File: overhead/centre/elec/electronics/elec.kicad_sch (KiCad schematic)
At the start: 135 parts, among them IC1 MAX7219CWG, J1 Conn_02x01, J2 Conn_02x20_Counter_Clockwise, P1 Conn_01x02, P2 DataIn

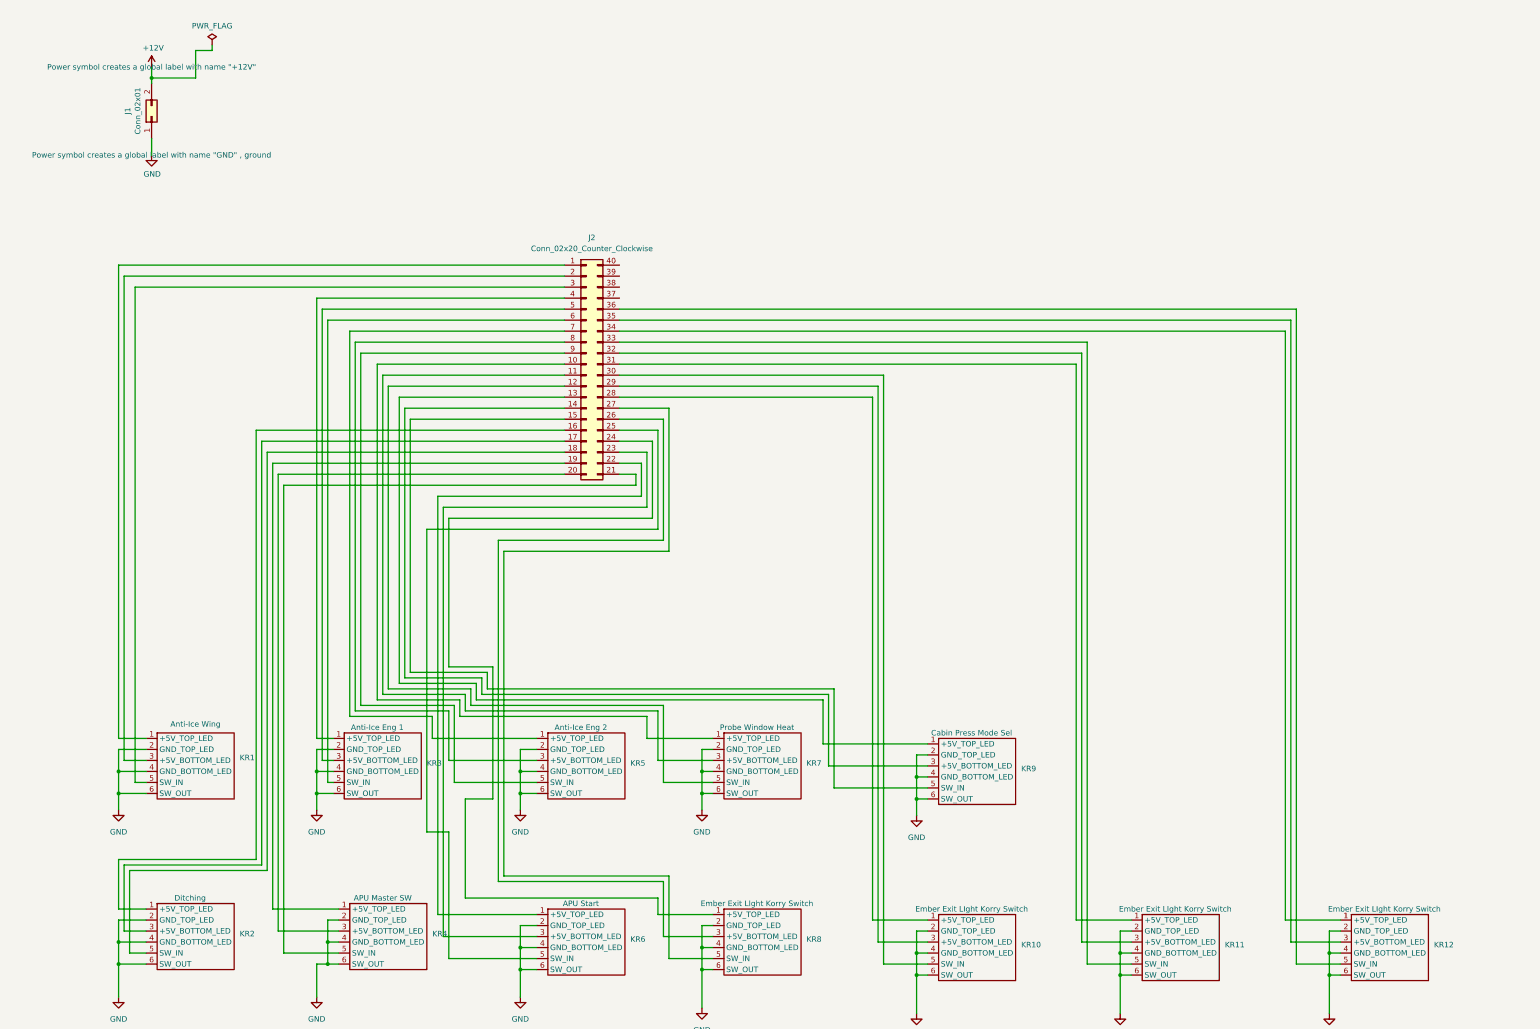
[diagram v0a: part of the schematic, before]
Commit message: Updated Panels ELEC
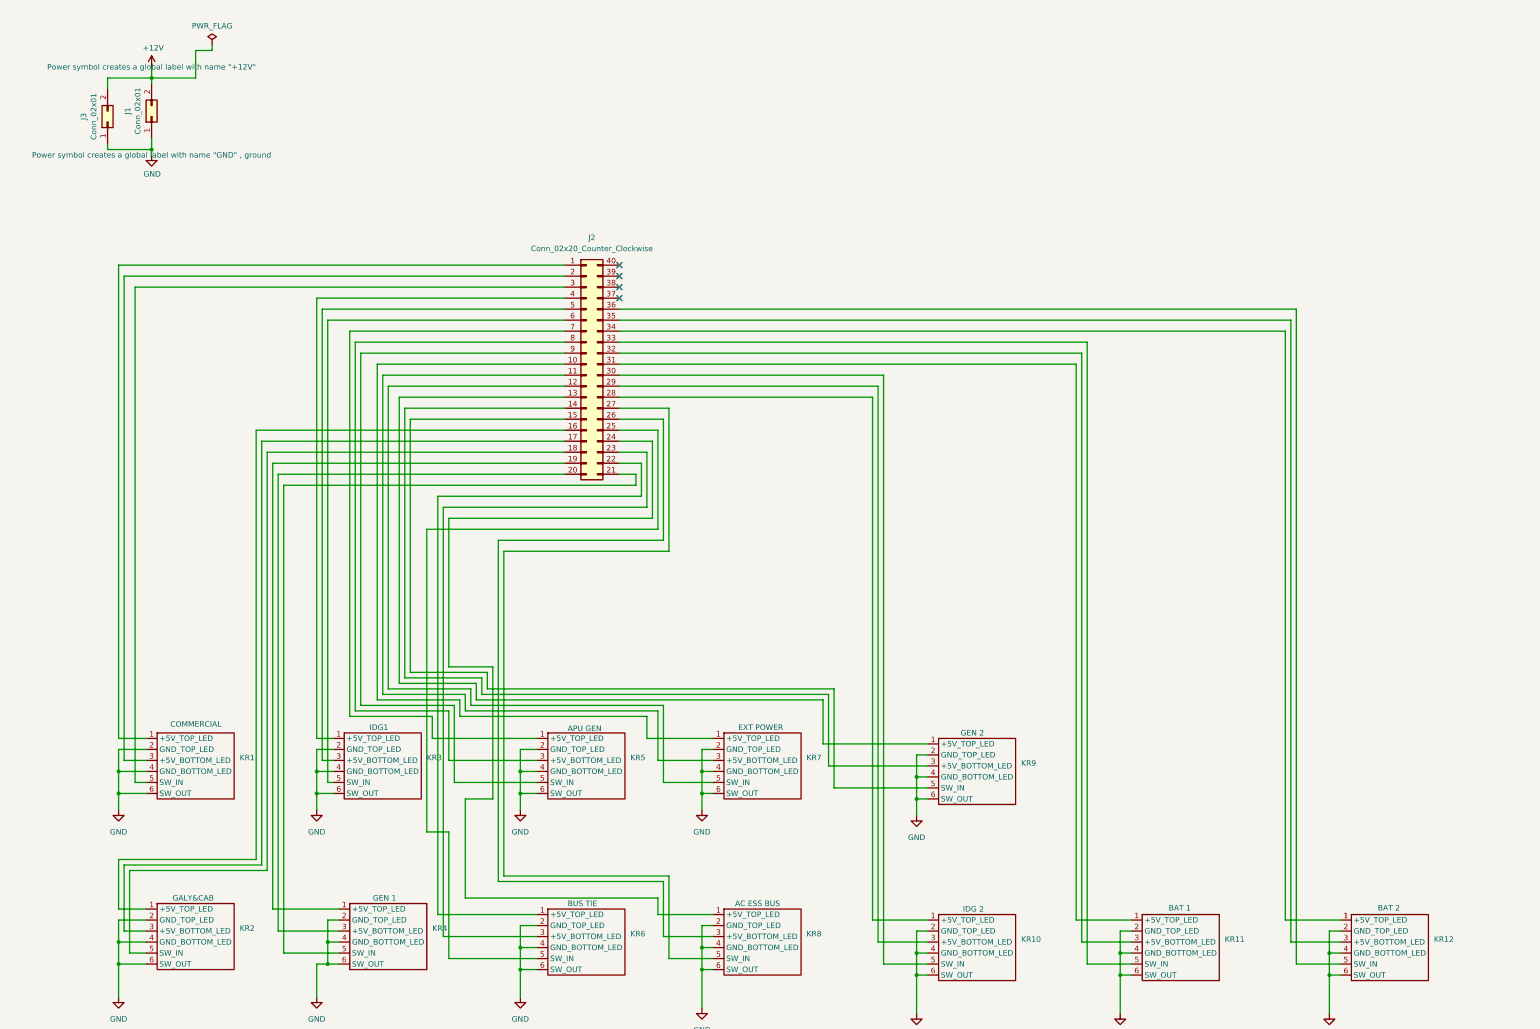
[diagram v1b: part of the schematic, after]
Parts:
- added J3: Conn_02x01, TerminalBlock:TerminalBlock_bornier-2_P5.08mm, symbol Connector_Generic:Conn_02x01
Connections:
- net +12V: now also J3.2 (Pin_2)
- net GND: now also J3.1 (Pin_1)
- no-connect marks 3 -> 7

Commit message: Changes
Changes
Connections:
- net at J2.24 (Pin_24): now also KR6.5 (SW_IN); no longer KR8.1 (+5V_TOP_LED)
- net at J2.25 (Pin_25): now also KR8.1 (+5V_TOP_LED); no longer KR6.5 (SW_IN)
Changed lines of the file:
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@@
 	(wire
 		(pts
+			(xy 170.18 218.44) (xy 170.18 217.17)
+		)
+		(stroke
+			(width 0)
+			(type default)
+		)
+	)
+	(wire
+		(pts
 			(xy 459.74 66.04) (xy 467.36 66.04)
 		)
@@
 	(wire
 		(pts
+			(xy 170.18 217.17) (xy 171.45 217.17)
+		)
+		(stroke
+			(width 0)
+			(type default)
+		)
+	)
+	(wire
+		(pts
 			(xy 581.66 220.98) (xy 604.52 220.98)
 		)
@@
 	(wire
 		(pts
-			(xy 170.18 219.71) (xy 162.56 219.71)
-		)
-		(stroke
-			(width 0)
-			(type default)
-		)
-	)
-	(wire
-		(pts
 			(xy 97.79 335.28) (xy 95.25 335.28)
 		)
@@
 	(wire
 		(pts
-			(xy 171.45 217.17) (xy 162.56 217.17)
-		)
-		(stroke
-			(width 0)
-			(type default)
-		)
-	)
-	(wire
-		(pts
 			(xy 511.81 104.14) (xy 519.43 104.14)
 		)
@@
 	(wire
 		(pts
+			(xy 165.1 218.44) (xy 170.18 218.44)
+		)
+		(stroke
+			(width 0)
+			(type default)
+		)
+	)
+	(wire
+		(pts
 			(xy 562.61 274.32) (xy 570.23 274.32)
 		)
@@
 	(wire
 		(pts
+			(xy 162.56 219.71) (xy 165.1 219.71)
+		)
+		(stroke
+			(width 0)
+			(type default)
+		)
+	)
+	(wire
+		(pts
 			(xy 238.76 106.68) (xy 262.89 106.68)
 		)
@@
 	(wire
 		(pts
+			(xy 167.64 217.17) (xy 162.56 217.17)
+		)
+		(stroke
+			(width 0)
+			(type default)
+		)
+	)
+	(wire
+		(pts
 			(xy 670.56 231.14) (xy 670.56 226.06)
 		)
@@
 	(wire
 		(pts
+			(xy 167.64 219.71) (xy 167.64 217.17)
+		)
+		(stroke
+			(width 0)
+			(type default)
+		)
+	)
+	(wire
+		(pts
 			(xy 257.81 69.85) (xy 257.81 96.52)
 		)
@@
 	(wire
 		(pts
+			(xy 165.1 219.71) (xy 165.1 218.44)
+		)
+		(stroke
+			(width 0)
+			(type default)
+		)
+	)
+	(wire
+		(pts
 			(xy 420.37 231.14) (xy 443.23 231.14)
 		)
@@
 		)
 		(stroke
+			(width 0)
+			(type default)
+		)
+	)
+	(wire
+		(pts
+			(xy 170.18 219.71) (xy 167.64 219.71)
+		)
+		(stroke
